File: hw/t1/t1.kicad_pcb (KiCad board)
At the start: 4 copper layers, 63.5 x 11.8 mm, 62 parts, among them J1 SFP edge (INF-8074i), J2 Rosenberger E6S20A-40MT5-Z (H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, U1 DP83TG720S-Q1 (or DP83TC812S-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, U2 STM32G031F6P6, U3 TPS62822DLC, Y1 25MHz CL8pF 2016

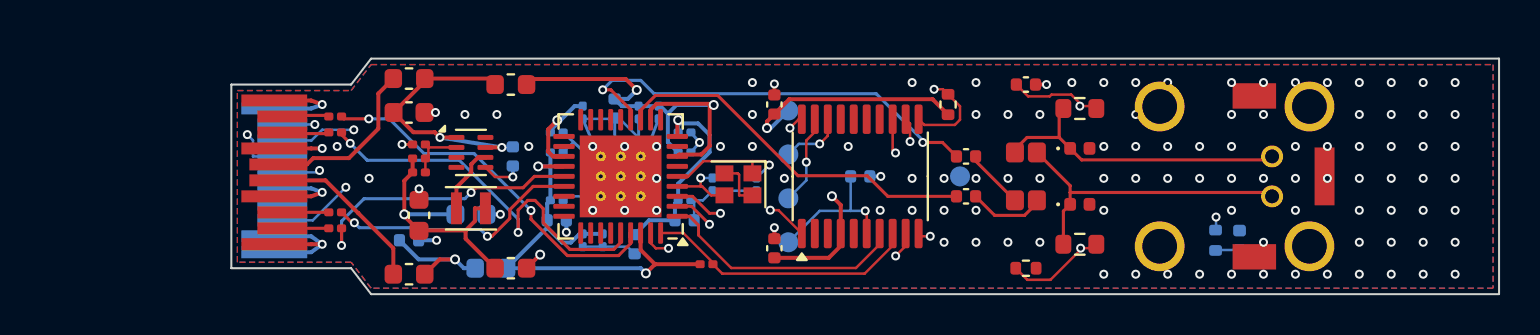
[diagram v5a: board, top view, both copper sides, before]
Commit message: t1: design-review fixes - coupled pairs by hand, F/GND/GND/B, load switch, two BOMs, CI
- every SGMII/MDI pair laid coupled (0.114/0.152, ~100 ohm diff) on one layer
  with matched vias; router does the slow nets only. Worst skew 1.08 mm (SG_RX)
- In2 is GND; slow signals may cross it except under the bottom-side pair
- SGMII lanes laid straight, polarity inverted in the PHY by the firmware
  (SGMII_CTRL_1 bits 7/8, TG720 and TC812)
- TPS22918 load switch on the 3.3 V entry (~3.6 ms soft start)
- 0.6 mm no-copper strip along every edge (mouse bites); escapes where it
  closed the router's way (U4 ON, MDC/INT/RST, VDD1P0, MCU GND, XO)
- jlc/bom.csv + cpl.csv replaced by bom/cpl-tg720 and bom/cpl-tc812
- fab/t1-1to1.pdf for the H-MTD print check
- KiCad 9: DRC 0, parity clean, ERC clean; only lib-revision warnings pass
- GitHub Actions: KiCad 9 check, firmware (4 variants, no warnings), gateware
- root README rewritten (11.8 mm body, current status, hardware-only checks)
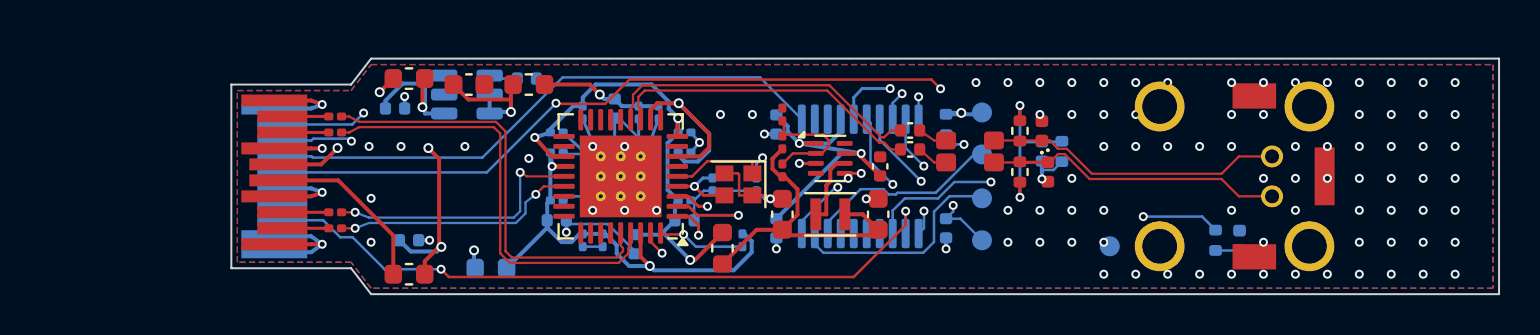
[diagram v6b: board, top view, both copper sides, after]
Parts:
- added C36: 2.2nF, Capacitor_SMD:C_0402_1005Metric, B.Cu at (114.8, 95.1)
- added C37: 10uF, Capacitor_SMD:C_0603_1608Metric, F.Cu at (111.9, 95.4)
- added U4: TPS22918DBVR, Package_TO_SOT_SMD:SOT-23-6, B.Cu at (111.8, 95.9)
- C1: value 10uF -> 1uF; footprint Capacitor_SMD:C_0603_1608Metric -> Capacitor_SMD:C_0402_1005Metric; moved to B.Cu
- C26, C28: moved to F.Cu
- C30, C31, C35, R1, R5, R8, U2: moved to B.Cu
- R6, R7: footprint Resistor_SMD:R_0603_1608Metric -> Resistor_SMD:R_0402_1005Metric
- moved C28 20.4 mm to (132.4, 101.9), turned to 90 degrees
- moved C26 18.4 mm to (132.5, 99.5), turned to 90 degrees
- moved R4 18.3 mm to (127.6, 96.9), turned to 90 degrees
- moved C29 18.2 mm to (127.6, 98.3), turned to 90 degrees
- moved R3 18.2 mm to (127.6, 99.7), turned to 90 degrees
- moved C27 18.2 mm to (127.6, 101.9)
- moved L1 18.0 mm to (130.0, 101.9)
- moved U3 18.0 mm to (130.0, 99.1)
- moved FB3 10.6 mm to (124.6, 103.6), turned to 90 degrees
- moved TP1 9.70 mm to (137.6, 96.8)
- moved TP4 9.70 mm to (137.6, 103.2)
- moved TP2 9.70 mm to (137.6, 98.9)
- moved TP3 9.70 mm to (137.6, 101.1)
- moved TP5 8.28 mm to (144.0, 103.5)
- moved R8 6.12 mm to (141.6, 98.8), turned to -90 degrees
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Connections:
- C1 pad 1: +3V3 -> VIN_RAW
- C2 pad 1: +3V3 -> VIN_RAW
- C3 pad 2: SG_TX_P -> SG_TX_N
- C4 pad 2: SG_TX_N -> SG_TX_P
- C5 pad 2: SG_RX_P -> SG_RX_N
- C6 pad 2: SG_RX_N -> SG_RX_P
- FB1 pad 2: +3V3 -> VIN_RAW
- FB2 pad 2: +3V3 -> VIN_RAW
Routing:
- net SCL: track 28.5 -> 48.8 mm, vias 2 -> 3
- net VIN_RAW: track 0.00 -> 19.8 mm, vias 0 -> 3
- net MDI_CT: track 16.8 -> 8.32 mm
- net NRST: track 7.40 -> 15.7 mm, vias 1 -> 2
- net SDA: track 35.8 -> 28.6 mm, vias 2 -> 0
- net SWDIO: track 3.19 -> 9.92 mm, vias 1 -> 0
- net TX_DISABLE: track 39.1 -> 45.8 mm, vias 2 -> 3
- net SWCLK: track 4.51 -> 11.2 mm, vias 1 -> 0
- net MDIO: track 13.7 -> 20.2 mm, vias 0 -> 2
- net TX_FAULT: track 41.2 -> 47.0 mm
- net TRD_P: track 21.9 -> 16.1 mm, vias 2 -> 0
- net MDC: track 12.5 -> 18.0 mm, vias 0 -> 2
- net VDD1P0: track 29.7 -> 24.4 mm
- net GND: track 56.3 -> 60.3 mm, vias 118 -> 106
- net SG_TX_N: track 18.4 -> 22.0 mm, vias 2 -> 0
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- added copper zone on In2.Cu, net GND
- removed copper zone on In2.Cu, net +3V3

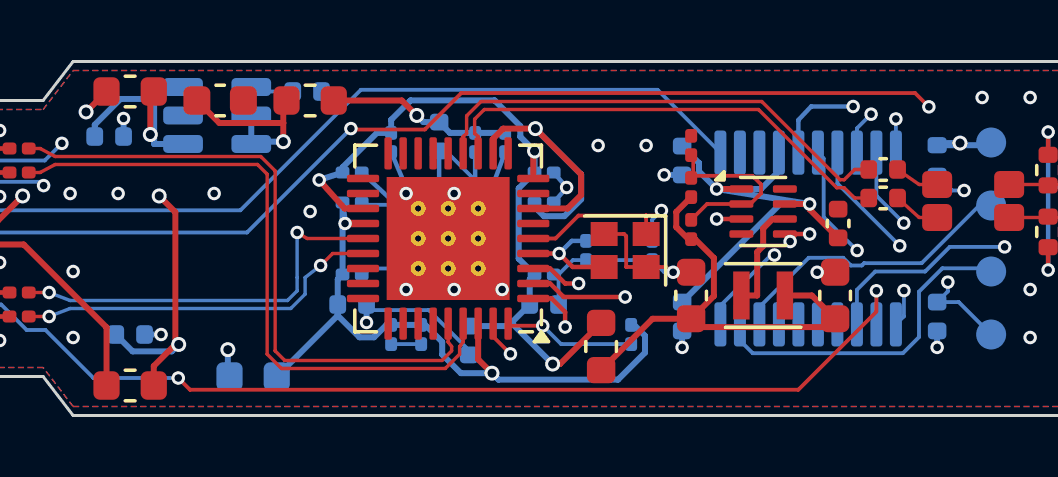
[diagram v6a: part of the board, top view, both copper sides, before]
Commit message: References checked against the design; the fixes they turned up
docs/REFERENCES.md: the standards, Linux drivers, TI / Realtek / Microchip /
Gowin datasheets, app notes and EVMs, and commercial modules, each with a
table of the design against it.

Fixed from it:
- T1S: CLKHOLD_N (K3) tied high - pulled down during configuration, it would
  have held the flash clock and the FPGA would never load; P1 (also
  SSPI_CS_N) pulled up (R26); AN1718 BIN: 0.75 W end-node resistors (were
  0.25 W), 100 V centre cap (was 50 V), no copper under the CMC
- RJ45 / T1S: buck inductor 1.0 uH (TPS6282x Table 3): the RTL8221B wants
  its core switcher out of pulse skipping, which now starts at ~0.15 A, not
  ~0.33 A
- T1: no copper under the CMC on F/In1 (DP83TG720 8.5); the TC812 loadout
  fits the 200 uH CMC its datasheet asks for
- fw: PHY settings 70 ms after reset release (TG720: 65 ms before the first
  MDIO frame) with the 0x56 bridge answering 0xFFFF until then; LAN8670 set-up
  picked by silicon revision (AN1699 Rev G: C2 or D0); collision detection
  follows PLCA as AN1699 asks

All three boards: DRC 0 / 0 unconnected, KiCad 9 PASS, panels clean.
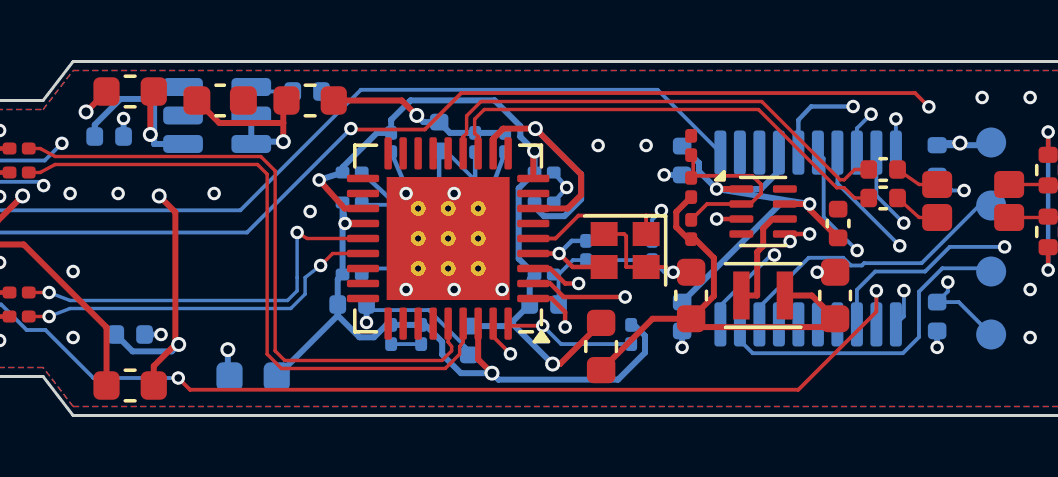
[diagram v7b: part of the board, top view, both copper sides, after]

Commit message: Review fixes: 100 V MDI DC block, 128 Mbit flash, T1S MDI geometry
- T1 C33/C34: 100 nF 100 V X5R 0402 (GRM155R62A104KE14D, C162178), split
  from the 16 V decap line (C1525) they had been grouped with
- T1 R6/R7: 1 k 1 % 0.2 W anti-surge 0402 (C313354) instead of 62.5 mW;
  still short of TI's 0.75 W 2010, documented
- T1S U2: GD25Q128EWIGR (C2982923), same WSON-8 footprint, so Gowin's
  default golden address 0x800000 is inside the part; ORDER.md gives the
  flash layout
- compliance.py: each lane's geometry comes from its routed track width;
  the T1S MDI is two 0.2 mm lines (Z0 44.8) with its own delay and loss,
  and an unsolved width now stops the run
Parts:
- C33, C34: value 100nF -> 100nF 100V
- R6, R7: value 1k 1% -> 1k 1% 0.2W
